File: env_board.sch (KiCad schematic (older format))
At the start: 9 parts, among them J1 CONN_01X07, U1 RFD77101, U2 ENS210, U3 CCS811, U6 BMP280

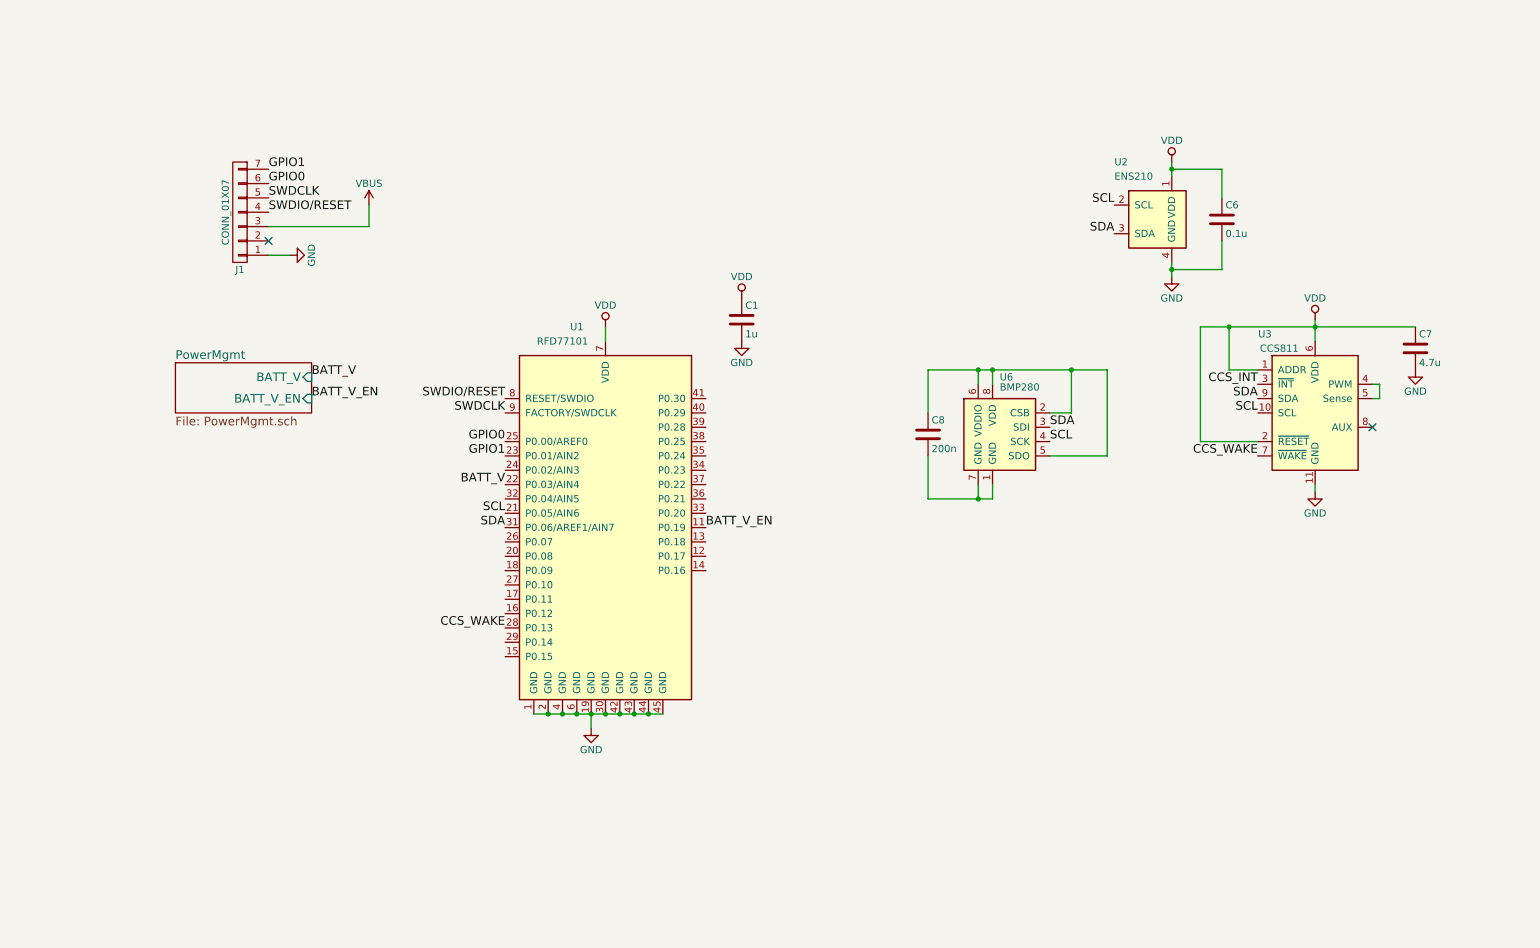
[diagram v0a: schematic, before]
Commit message: changes to use nRF52840 instead of simblee
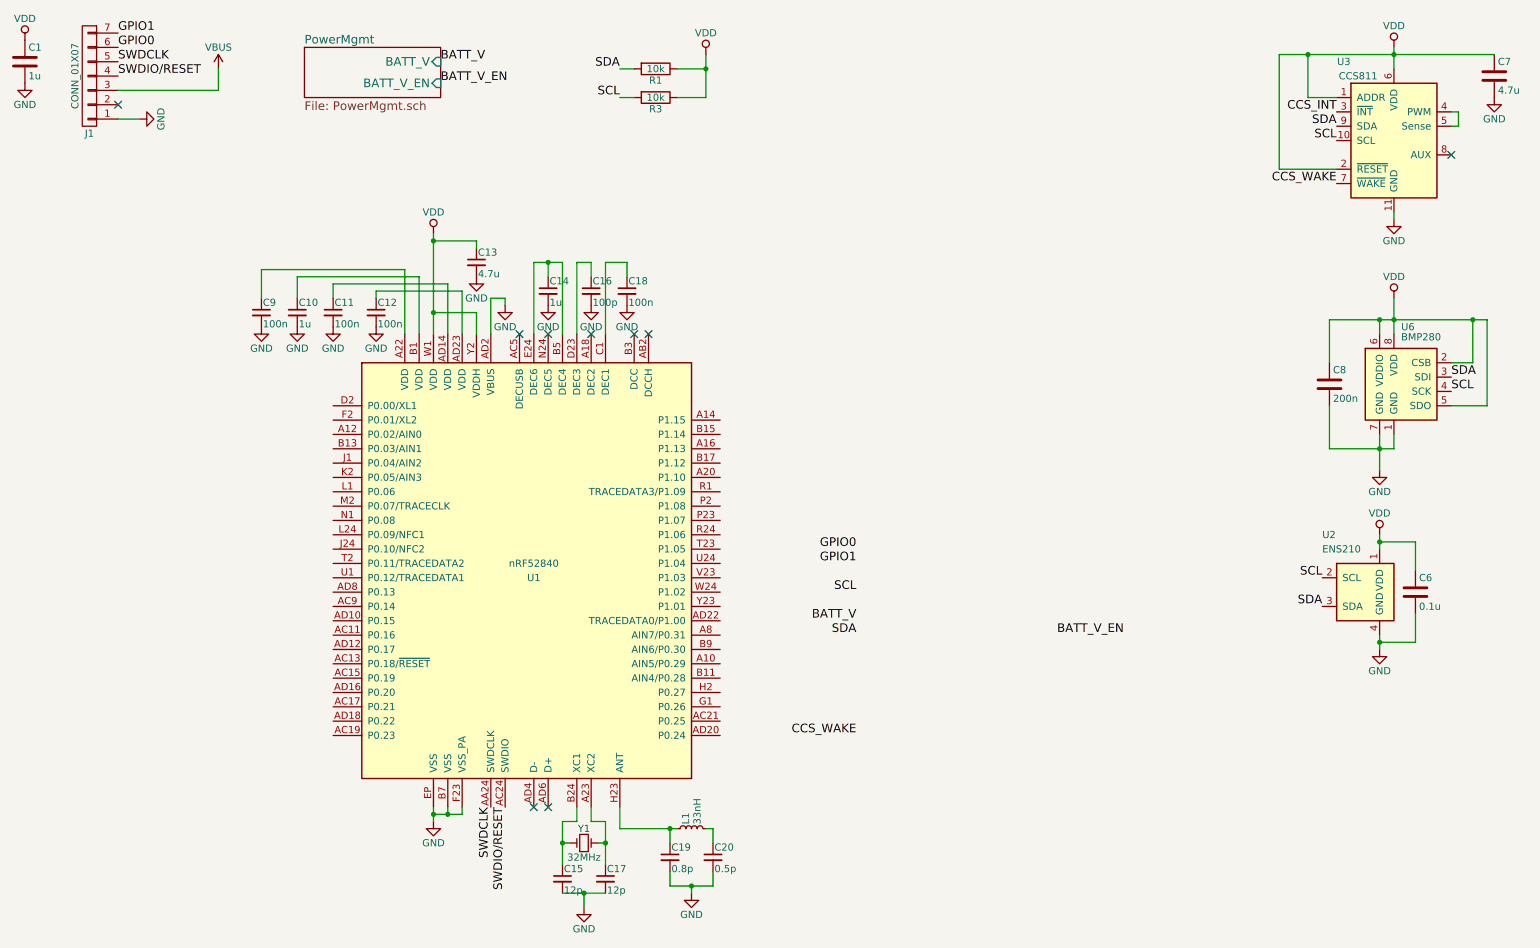
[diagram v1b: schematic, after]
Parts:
- removed U1: RFD77101, kicad-RF_Modules:RFDigital_RFD77101, symbol RFD77101
- added C10, C14: 1u, Capacitors_SMD:C_0603, symbol C_Small
- added C11, C12, C18, C9: 100n, Capacitors_SMD:C_0603, symbol C_Small
- added C13: 4.7u, Capacitors_SMD:C_0603, symbol C_Small
- added C15, C17: 12p, Capacitors_SMD:C_0603, symbol C_Small
- added C16: 100p, Capacitors_SMD:C_0603, symbol C_Small
- added C19: 0.8p, Capacitors_SMD:C_0603, symbol C_Small
- added C20: 0.5p, Capacitors_SMD:C_0603, symbol C_Small
- added L1: 33nH, Capacitors_SMD:C_0603, symbol L_Small
- added R1, R3: 10k, Resistors_SMD:R_0603, symbol R
- added U1: nRF52840, Package_DFN_QFN:Nordic_AQFN-73-1EP_7x7mm_P0.5mm, symbol nRF52840-RESCUE-env_board
- added Y1: 32MHz, Crystals:Crystal_SMD_0603_4Pads, symbol Crystal_Small
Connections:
- net GND: now also C8.2, U6.1 (GND), U6.7 (GND), C10.2, C11.2, C12.2, C13.2, C14.2, C15.2, C16.2, C17.2, C18.2, C19.2, C20.2, C9.2, U1.AD2 (VBUS), U1.B7 (VSS), U1.EP (VSS), U1.F23 (VSS_PA)
- net SCL: now also R3.2
- net SDA: now also R1.2
- net SWDCLK: now also U1.AA24 (SWDCLK)
- net SWDIO/RESET: now also U1.AC24 (SWDIO)
- net VDD: now also C8.1, U6.2 (CSB), U6.5 (SDO), U6.6 (VDDIO), U6.8 (VDD), C13.1, R1.1, R3.1, U1.W1 (VDD), U1.Y2 (VDDH)
- new net: C9.1, U1.A22 (VDD)
- new net: C17.1, U1.A23 (XC2), Y1.2
- new net: C11.1, U1.AD14 (VDD)
- new net: C12.1, U1.AD23 (VDD)
- new net: C10.1, U1.B1 (VDD)
- new net: C15.1, U1.B24 (XC1), Y1.1
- new net: C14.1, U1.B5 (DEC4), U1.E24 (DEC6)
- new net: C18.1, U1.C1 (DEC1)
- new net: C16.1, U1.D23 (DEC3)
- new net: C19.1, L1.1, U1.H23 (ANT)
- new net: C20.1, L1.2
- no-connect marks 2 -> 9
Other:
- moved on the sheet: C1, C6, C7, C8, J1, U2, U3, U6
